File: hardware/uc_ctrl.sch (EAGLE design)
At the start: 41 parts, among them Q4 si2305cd, Q7 si2305cd, T1 BC846, T3 BC846, U1 3vLDO, Y1 32768Hz CFPX-217 12.5pF

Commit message: cleanup
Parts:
- added U$8: RESETTABLE, Simplex-Fuses:RESETTABLE
- R16, R20: value 100k -> 100K
- R19, R21: value 47k -> 220K
- R22: value 1K -> 500K
- SJ1: value (none) -> pow
- U$3: value MOLEX_4HORIZONTAL -> uCurrent
- U$6: value MOLEX_2HORIZONTAL -> power
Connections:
- new net N$9: U$6.2, U$8.P$2
- net VCC_IN: now also U$8.P$1; no longer U$6.2
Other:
- moved on the sheet: C8, C9, U$6
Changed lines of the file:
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@@
 <part name="Q4" library="Simplex-DiscreteSemi" deviceset="MOSFET-PCHANNEL" device="SMD_POWER" value="si2305cd"/>
 <part name="T1" library="transistor" deviceset="BC846" device=""/>
-<part name="R16" library="rcl" deviceset="R-EU_" device="R0805W" value="100k"/>
+<part name="R16" library="rcl" deviceset="R-EU_" device="R0805W" value="100K"/>
 <part name="GND48" library="SparkFun" deviceset="GND" device=""/>
-<part name="R19" library="rcl" deviceset="R-EU_" device="R0805W" value="47k"/>
+<part name="R19" library="rcl" deviceset="R-EU_" device="R0805W" value="220K"/>
 <part name="Q7" library="Simplex-DiscreteSemi" deviceset="MOSFET-PCHANNEL" device="SMD_POWER" value="si2305cd"/>
 <part name="T3" library="transistor" deviceset="BC846" device=""/>
-<part name="R20" library="rcl" deviceset="R-EU_" device="R0805W" value="100k"/>
+<part name="R20" library="rcl" deviceset="R-EU_" device="R0805W" value="100K"/>
 <part name="GND49" library="SparkFun" deviceset="GND" device=""/>
-<part name="R21" library="rcl" deviceset="R-EU_" device="R0805W" value="47k"/>
-<part name="R22" library="rcl" deviceset="R-EU_" device="R0805W" value="1K"/>
+<part name="R21" library="rcl" deviceset="R-EU_" device="R0805W" value="220K"/>
+<part name="R22" library="rcl" deviceset="R-EU_" device="R0805W" value="500K"/>
 <part name="R24" library="rcl" deviceset="R-EU_" device="R0805W" value="1M"/>
 <part name="GND34" library="SparkFun" deviceset="GND" device=""/>
@@
 <part name="R2" library="rcl" deviceset="R-EU_" device="R0805W" value="100k"/>
 <part name="GND7" library="SparkFun" deviceset="GND" device=""/>
-<part name="SJ1" library="SparkFun-Passives" deviceset="SOLDERJUMPER_2WAY" device="PASTE1&amp;2"/>
+<part name="SJ1" library="SparkFun-Passives" deviceset="SOLDERJUMPER_2WAY" device="PASTE1&amp;2" value="pow"/>
 <part name="SJ2" library="SparkFun-Passives" deviceset="SOLDERJUMPER" device="NC2"/>
-<part name="U$3" library="Simplex-Connectors" deviceset="MOLEX_4" device="HORIZONTAL"/>
-<part name="U$6" library="Simplex-Connectors" deviceset="MOLEX_2" device="HORIZONTAL"/>
+<part name="U$3" library="Simplex-Connectors" deviceset="MOLEX_4" device="HORIZONTAL" value="uCurrent"/>
+<part name="U$6" library="Simplex-Connectors" deviceset="MOLEX_2" device="HORIZONTAL" value="power"/>
+<part name="GND5" library="SparkFun" deviceset="GND" device=""/>
+<part name="U$8" library="Simplex-Fuses" deviceset="RESETTABLE" device=""/>
 </parts>
 <sheets>
@@
 <plain>
 <text x="281.94" y="7.62" size="3.81" layer="97">02</text>
-<text x="144.78" y="53.34" size="1.778" layer="97">uC pins: 7 11 28</text>
+<text x="144.78" y="83.82" size="1.778" layer="97">uC pins: 7 11 28</text>
 <text x="215.9" y="129.54" size="1.778" layer="97">jumper settings:
 if Vcc_in is between 2.8-3.0 V
@@
 <instance part="GND30" gate="1" x="142.24" y="12.7"/>
 <instance part="SUPPLY11" gate="G$1" x="160.02" y="35.56"/>
-<instance part="SUPPLY12" gate="G$1" x="152.4" y="81.28"/>
-<instance part="C8" gate="G$1" x="152.4" y="68.58" rot="R180"/>
-<instance part="GND13" gate="1" x="152.4" y="60.96"/>
-<instance part="C9" gate="G$1" x="160.02" y="68.58" rot="R180"/>
-<instance part="GND10" gate="1" x="160.02" y="60.96"/>
+<instance part="SUPPLY12" gate="G$1" x="152.4" y="111.76"/>
+<instance part="C8" gate="G$1" x="152.4" y="99.06" rot="R180"/>
+<instance part="GND13" gate="1" x="152.4" y="91.44"/>
+<instance part="C9" gate="G$1" x="160.02" y="99.06" rot="R180"/>
+<instance part="GND10" gate="1" x="160.02" y="91.44"/>
 <instance part="GND41" gate="1" x="78.74" y="106.68"/>
 <instance part="C1" gate="G$1" x="238.76" y="93.98"/>
@@
 <instance part="SJ2" gate="1" x="124.46" y="165.1"/>
 <instance part="U$3" gate="G$1" x="254" y="96.52"/>
-<instance part="U$6" gate="G$1" x="254" y="93.98" rot="MR180"/>
+<instance part="U$6" gate="G$1" x="160.02" y="66.04" rot="MR180"/>
+<instance part="GND5" gate="1" x="152.4" y="55.88"/>
+<instance part="U$8" gate="G$1" x="144.78" y="68.58"/>
 </instances>
 <busses>
@@
 <pinref part="C8" gate="G$1" pin="1"/>
 <pinref part="GND13" gate="1" pin="GND"/>
-<wire x1="152.4" y1="66.04" x2="152.4" y2="63.5" width="0.1524" layer="91"/>
+<wire x1="152.4" y1="96.52" x2="152.4" y2="93.98" width="0.1524" layer="91"/>
 </segment>
 <segment>
 <pinref part="C9" gate="G$1" pin="1"/>
 <pinref part="GND10" gate="1" pin="GND"/>
-<wire x1="160.02" y1="66.04" x2="160.02" y2="63.5" width="0.1524" layer="91"/>
+<wire x1="160.02" y1="96.52" x2="160.02" y2="93.98" width="0.1524" layer="91"/>
 </segment>
 <segment>
@@
 </segment>
 <segment>
-<wire x1="248.92" y1="104.14" x2="248.92" y2="91.44" width="0.1524" layer="91"/>
+<wire x1="248.92" y1="104.14" x2="248.92" y2="86.36" width="0.1524" layer="91"/>
 <pinref part="GND4" gate="1" pin="GND"/>
-<wire x1="248.92" y1="91.44" x2="248.92" y2="86.36" width="0.1524" layer="91"/>
 <wire x1="248.92" y1="104.14" x2="254" y2="104.14" width="0.1524" layer="91"/>
-<wire x1="254" y1="91.44" x2="248.92" y2="91.44" width="0.1524" layer="91"/>
-<junction x="248.92" y="91.44"/>
 <pinref part="U$3" gate="G$1" pin="1"/>
-<pinref part="U$6" gate="G$1" pin="1"/>
+<label x="251.46" y="104.14" size="1.778" layer="95"/>
+<label x="152.4" y="63.5" size="1.778" layer="95"/>
 </segment>
 <segment>
@@
 <wire x1="27.94" y1="22.86" x2="25.4" y2="22.86" width="0.1524" layer="91"/>
 <wire x1="25.4" y1="22.86" x2="25.4" y2="15.24" width="0.1524" layer="91"/>
+</segment>
+<segment>
+<pinref part="U$6" gate="G$1" pin="1"/>
+<pinref part="GND5" gate="1" pin="GND"/>
+<wire x1="160.02" y1="63.5" x2="152.4" y2="63.5" width="0.1524" layer="91"/>
+<wire x1="152.4" y1="63.5" x2="152.4" y2="58.42" width="0.1524" layer="91"/>
 </segment>
 </net>
@@
 <segment>
 <pinref part="SUPPLY12" gate="G$1" pin="VCC"/>
-<wire x1="152.4" y1="76.2" x2="152.4" y2="78.74" width="0.1524" layer="91"/>
+<wire x1="152.4" y1="106.68" x2="152.4" y2="109.22" width="0.1524" layer="91"/>
 <pinref part="C8" gate="G$1" pin="2"/>
-<wire x1="152.4" y1="76.2" x2="152.4" y2="73.66" width="0.1524" layer="91"/>
-<junction x="152.4" y="76.2"/>
+<wire x1="152.4" y1="106.68" x2="152.4" y2="104.14" width="0.1524" layer="91"/>
+<junction x="152.4" y="106.68"/>
 <pinref part="C9" gate="G$1" pin="2"/>
-<wire x1="160.02" y1="73.66" x2="160.02" y2="76.2" width="0.1524" layer="91"/>
-<wire x1="160.02" y1="76.2" x2="152.4" y2="76.2" width="0.1524" layer="91"/>
+<wire x1="160.02" y1="104.14" x2="160.02" y2="106.68" width="0.1524" layer="91"/>
+<wire x1="160.02" y1="106.68" x2="152.4" y2="106.68" width="0.1524" layer="91"/>
 </segment>
 <segment>
@@
 <junction x="238.76" y="101.6"/>
 <pinref part="U$3" gate="G$1" pin="2"/>
+<label x="243.84" y="101.6" size="1.778" layer="95"/>
 </segment>
 </net>
@@
 </segment>
 <segment>
-<wire x1="254" y1="93.98" x2="243.84" y2="93.98" width="0.1524" layer="91"/>
-<label x="243.84" y="93.98" size="1.778" layer="95"/>
-<pinref part="U$6" gate="G$1" pin="2"/>
+<label x="132.08" y="68.58" size="1.778" layer="95"/>
+<pinref part="U$8" gate="G$1" pin="P$1"/>
+<wire x1="139.7" y1="68.58" x2="132.08" y2="68.58" width="0.1524" layer="91"/>
 </segment>
 <segment>
 <wire x1="208.28" y1="106.68" x2="205.74" y2="106.68" width="0.1524" layer="91"/>
 <wire x1="205.74" y1="106.68" x2="205.74" y2="111.76" width="0.1524" layer="91"/>
-<label x="203.2" y="111.76" size="1.778" layer="95"/>
+<label x="203.2" y="114.3" size="1.778" layer="95"/>
 <pinref part="SJ1" gate="G$1" pin="3"/>
-<wire x1="205.74" y1="111.76" x2="203.2" y2="111.76" width="0.1524" layer="91"/>
 </segment>
 </net>
@@
 </segment>
 </net>
+<net name="N$9" class="0">
+<segment>
+<pinref part="U$8" gate="G$1" pin="P$2"/>
+<wire x1="149.86" y1="68.58" x2="152.4" y2="68.58" width="0.1524" layer="91"/>
+<wire x1="152.4" y1="68.58" x2="152.4" y2="66.04" width="0.1524" layer="91"/>
+<pinref part="U$6" gate="G$1" pin="2"/>
+<wire x1="152.4" y1="66.04" x2="160.02" y2="66.04" width="0.1524" layer="91"/>
+</segment>
+</net>
 </nets>
 </sheet>
 </sheets>
+<errors>
+</errors>
 </schematic>
 </drawing>

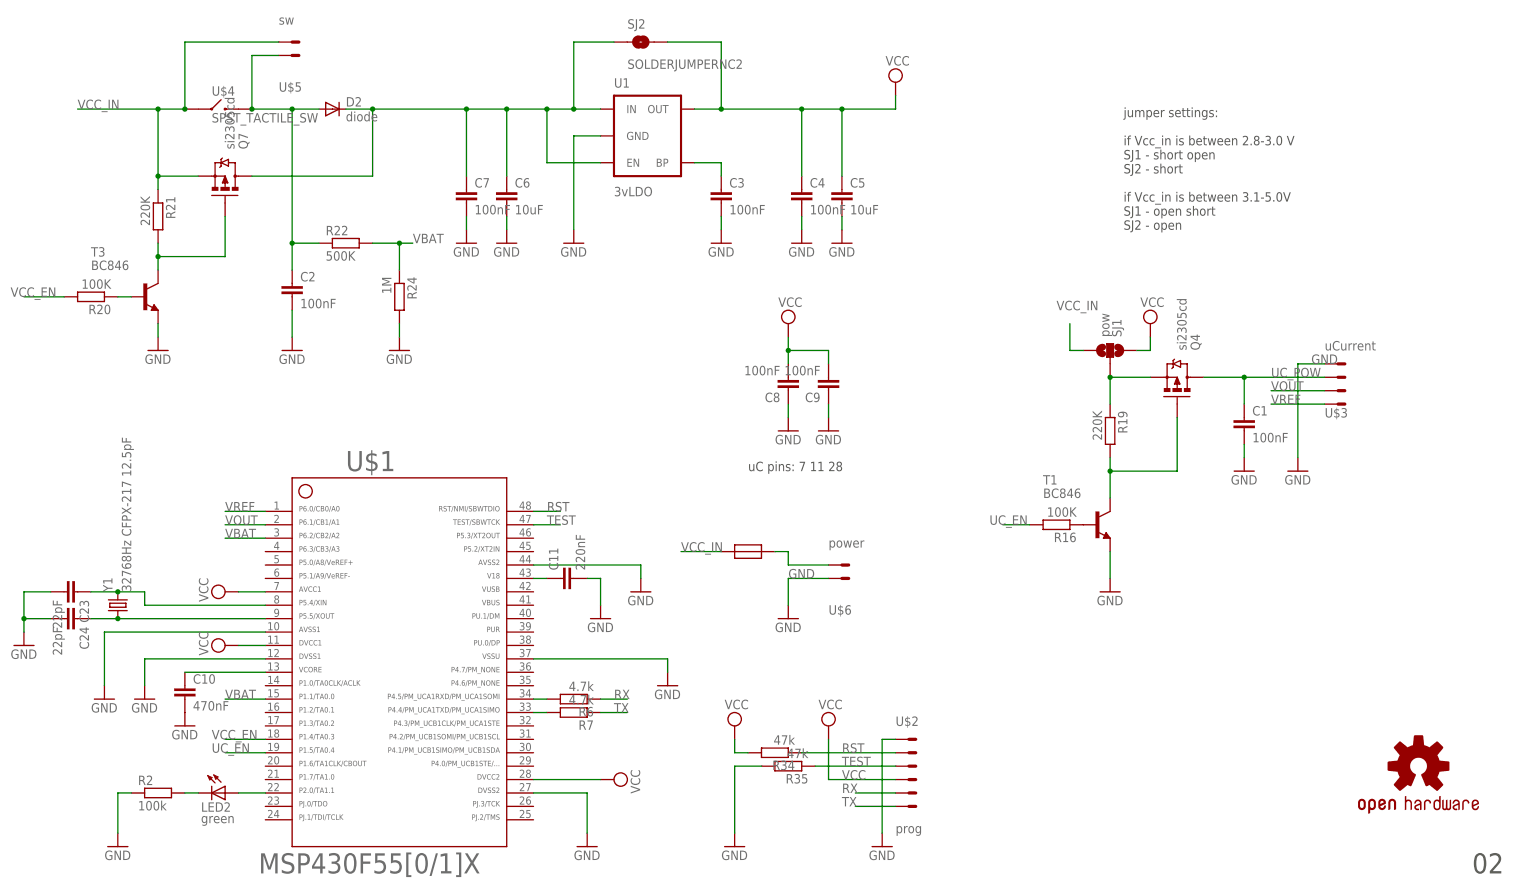
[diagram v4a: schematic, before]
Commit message: add 16bit adc
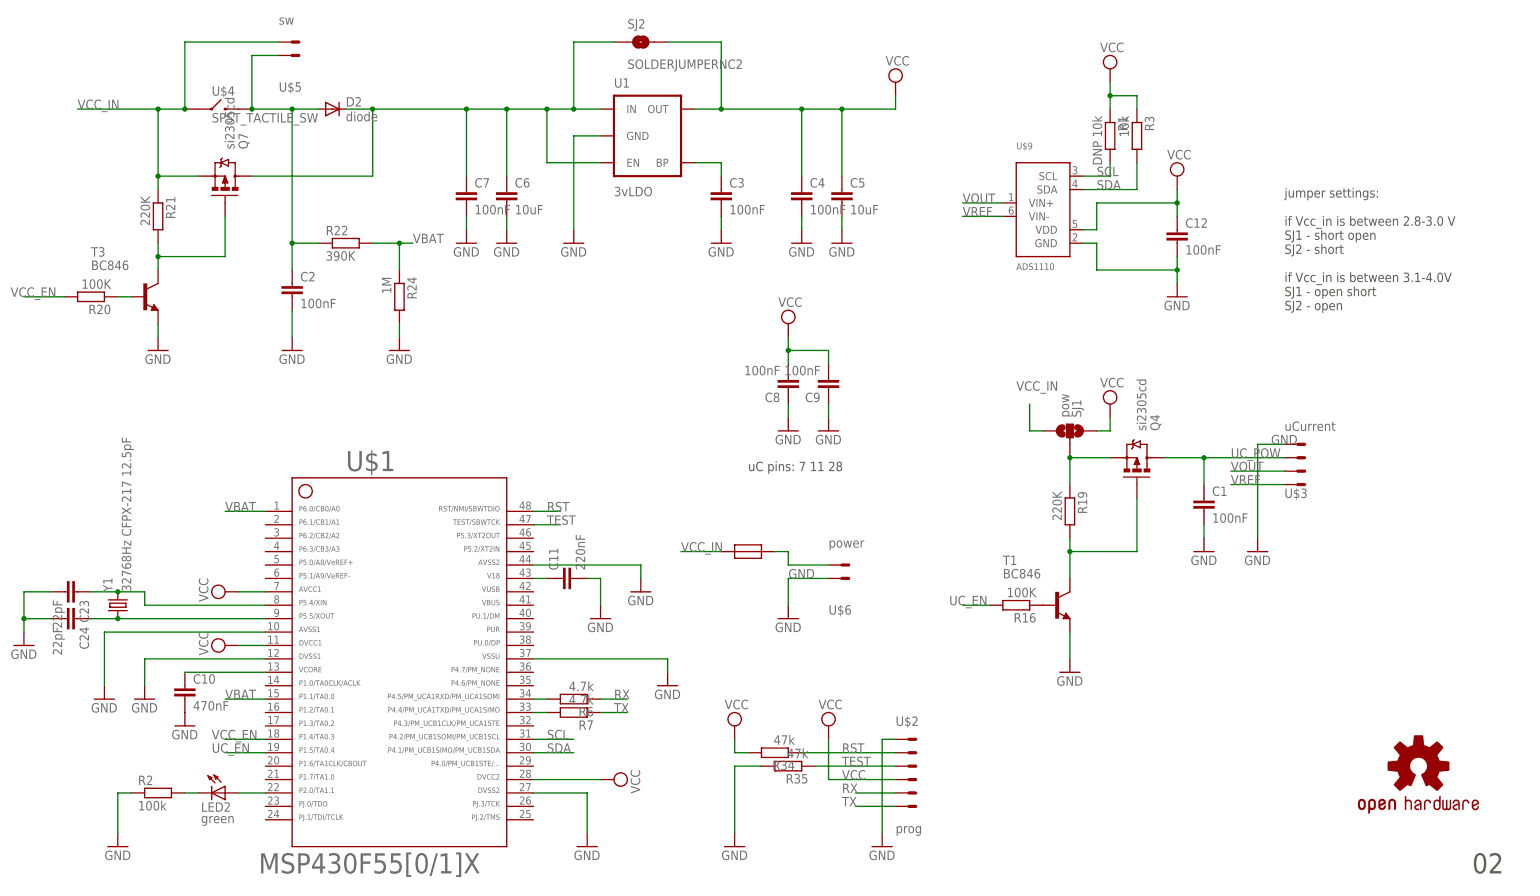
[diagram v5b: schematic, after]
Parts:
- added C12: 100nF, rcl:C-EUC0805
- added R1: DNP 10k, rcl:R-EU_R0805W
- added R3: 10k, rcl:R-EU_R0805W
- added U$9: ADS1110, Simplex-ICs:ADS1110
- R22: value 500K -> 390K
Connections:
- new net SCL: R1.2, U$1.31, U$9.SCL
- new net SDA: R3.2, U$1.30, U$9.SDA
- net GND: now also C12.2, U$9.GND
- net VBAT: now also U$1.1; no longer U$1.3
- net VCC: now also C12.1, R1.1, R3.1, U$9.VDD
- net VOUT: now also U$9.VIN+; no longer U$1.2
- net VREF: now also U$9.VIN-; no longer U$1.1
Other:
- note added: "jumper settings: if Vcc_in is between 2.8-3.0 V SJ1 - short open SJ2 - short if Vcc_in is between 3.1-4.0V SJ1 - open short SJ2 - open"
- note removed: "jumper settings: if Vcc_in is between 2.8-3.0 V SJ1 - short open SJ2 - short if Vcc_in is between 3.1-5.0V SJ1 - open short SJ2 - open"
- moved on the sheet: C1, Q4, R16, R19, SJ1, T1, U$3

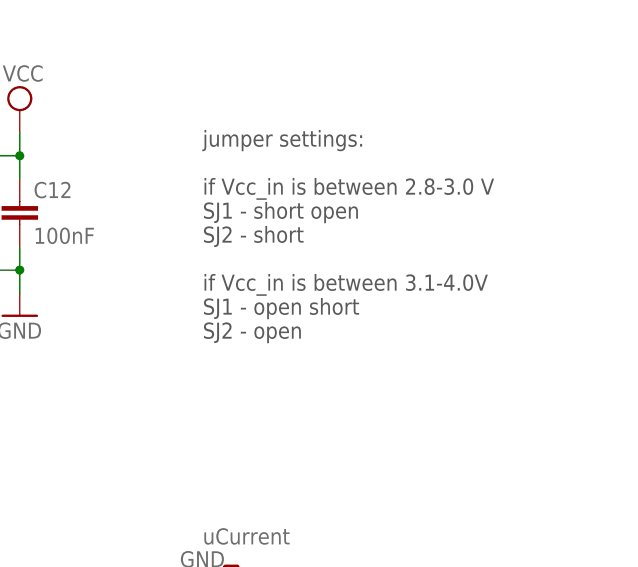
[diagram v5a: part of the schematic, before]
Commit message: sent gerbers to manufacturer
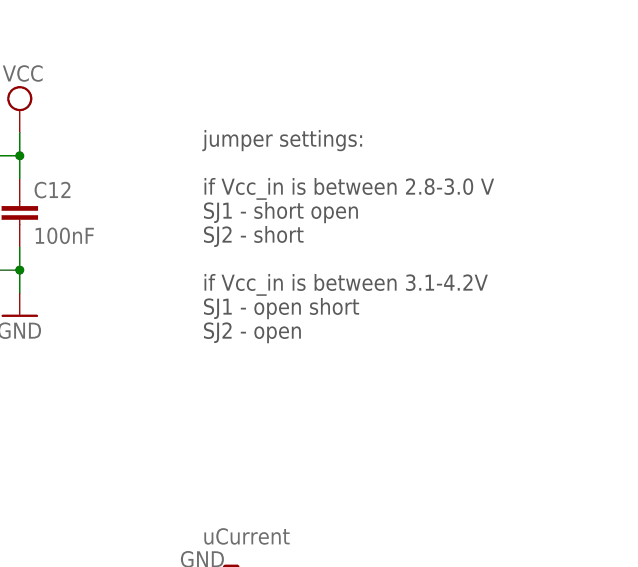
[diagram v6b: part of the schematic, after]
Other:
- note added: "jumper settings: if Vcc_in is between 2.8-3.0 V SJ1 - short open SJ2 - short if Vcc_in is between 3.1-4.2V SJ1 - open short SJ2 - open"
- note removed: "jumper settings: if Vcc_in is between 2.8-3.0 V SJ1 - short open SJ2 - short if Vcc_in is between 3.1-4.0V SJ1 - open short SJ2 - open"
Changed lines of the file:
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@@
 SJ1 - short open
 SJ2 - short
-if Vcc_in is between 3.1-4.0V
+if Vcc_in is between 3.1-4.2V
 SJ1 - open short
 SJ2 - open

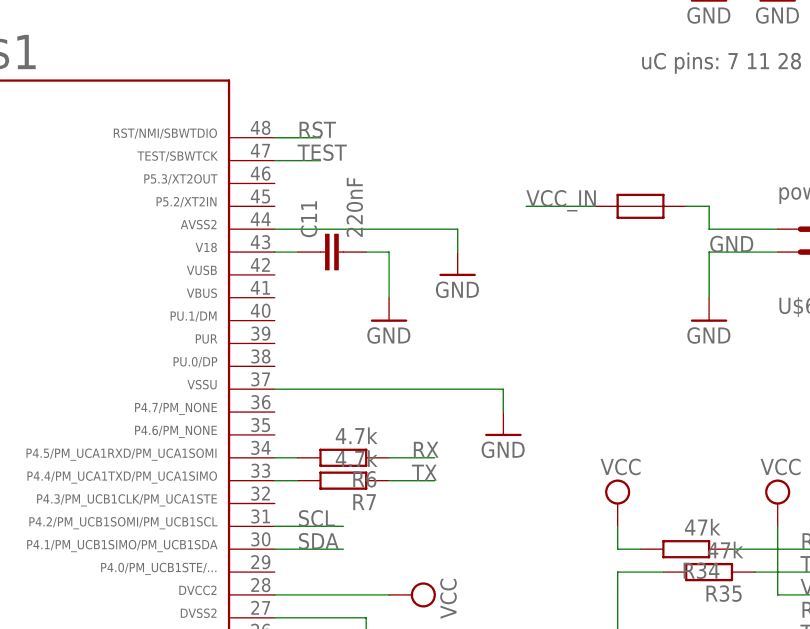
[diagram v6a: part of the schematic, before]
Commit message: unused pin tweaks
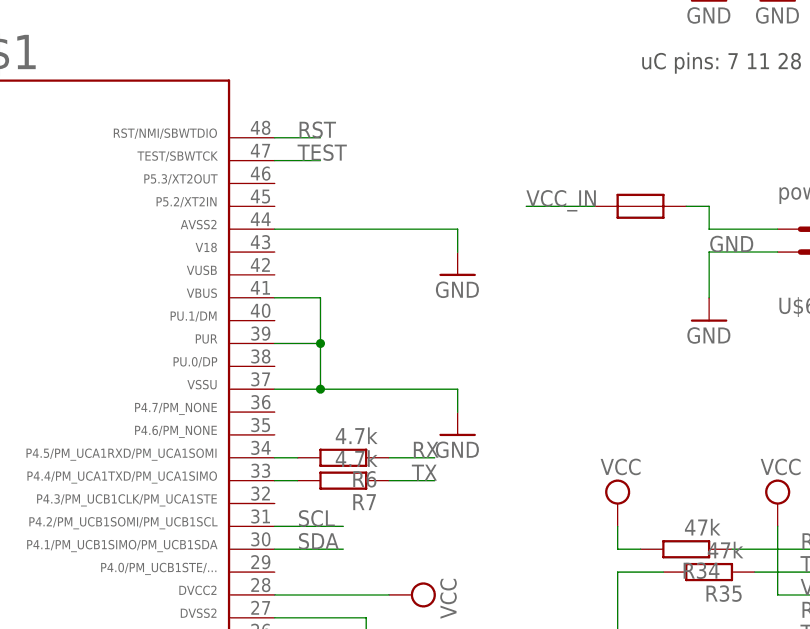
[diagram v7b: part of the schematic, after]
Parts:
- removed C11: 220nF, rcl:C-EUC0805
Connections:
- removed net N$7: C11.1, U$1.43
- net GND: now also U$1.39, U$1.41; no longer C11.2
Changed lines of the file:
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@@
 <part name="GND22" library="SparkFun" deviceset="GND" device=""/>
 <part name="C10" library="rcl" deviceset="C-EU" device="C0805" value="470nF"/>
-<part name="C11" library="rcl" deviceset="C-EU" device="C0805" value="220nF"/>
-<part name="GND23" library="SparkFun" deviceset="GND" device=""/>
 <part name="GND24" library="SparkFun" deviceset="GND" device=""/>
 <part name="R6" library="rcl" deviceset="R-EU_" device="R0805W" value="4.7k"/>
@@
 <instance part="GND22" gate="1" x="38.1" y="35.56"/>
 <instance part="C10" gate="G$1" x="38.1" y="43.18"/>
-<instance part="C11" gate="G$1" x="109.22" y="63.5" rot="R90"/>
-<instance part="GND23" gate="1" x="116.84" y="55.88"/>
-<instance part="GND24" gate="1" x="129.54" y="43.18"/>
+<instance part="GND24" gate="1" x="124.46" y="43.18"/>
 <instance part="R6" gate="G$1" x="111.76" y="40.64" rot="R180"/>
 <instance part="R7" gate="G$1" x="111.76" y="38.1" rot="R180"/>
@@
 <pinref part="U$1" gate="G$1" pin="37"/>
 <pinref part="GND24" gate="1" pin="GND"/>
-<wire x1="104.14" y1="48.26" x2="129.54" y2="48.26" width="0.1524" layer="91"/>
-<wire x1="129.54" y1="48.26" x2="129.54" y2="45.72" width="0.1524" layer="91"/>
+<wire x1="104.14" y1="48.26" x2="109.22" y2="48.26" width="0.1524" layer="91"/>
+<wire x1="109.22" y1="48.26" x2="124.46" y2="48.26" width="0.1524" layer="91"/>
+<wire x1="124.46" y1="48.26" x2="124.46" y2="45.72" width="0.1524" layer="91"/>
+<pinref part="U$1" gate="G$1" pin="39"/>
+<wire x1="104.14" y1="53.34" x2="109.22" y2="53.34" width="0.1524" layer="91"/>
+<wire x1="109.22" y1="53.34" x2="109.22" y2="48.26" width="0.1524" layer="91"/>
+<pinref part="U$1" gate="G$1" pin="41"/>
+<wire x1="104.14" y1="58.42" x2="109.22" y2="58.42" width="0.1524" layer="91"/>
+<wire x1="109.22" y1="58.42" x2="109.22" y2="53.34" width="0.1524" layer="91"/>
+<junction x="109.22" y="53.34"/>
+<junction x="109.22" y="48.26"/>
 </segment>
 <segment>
@@
 <label x="243.84" y="88.9" size="1.778" layer="95"/>
 <label x="152.4" y="63.5" size="1.778" layer="95"/>
-</segment>
-<segment>
-<pinref part="C11" gate="G$1" pin="2"/>
-<wire x1="114.3" y1="63.5" x2="116.84" y2="63.5" width="0.1524" layer="91"/>
-<wire x1="116.84" y1="63.5" x2="116.84" y2="58.42" width="0.1524" layer="91"/>
-<pinref part="GND23" gate="1" pin="GND"/>
 </segment>
 <segment>
@@
 </segment>
 </net>
-<net name="N$7" class="0">
-<segment>
-<pinref part="U$1" gate="G$1" pin="43"/>
-<pinref part="C11" gate="G$1" pin="1"/>
-<wire x1="106.68" y1="63.5" x2="104.14" y2="63.5" width="0.1524" layer="91"/>
-</segment>
-</net>
